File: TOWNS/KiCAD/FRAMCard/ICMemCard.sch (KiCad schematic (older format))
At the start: 15 parts, among them J1 PCMCIA_Connector, Q1 BC846X, Q2 BC846X, U1 FM18W08-SGTR, U2 FM18W08-SGTR

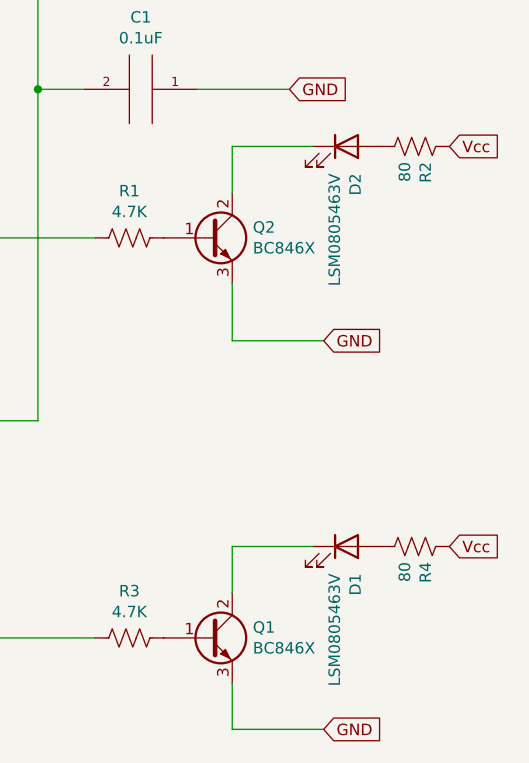
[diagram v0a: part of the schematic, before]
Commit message: Updated resistance.
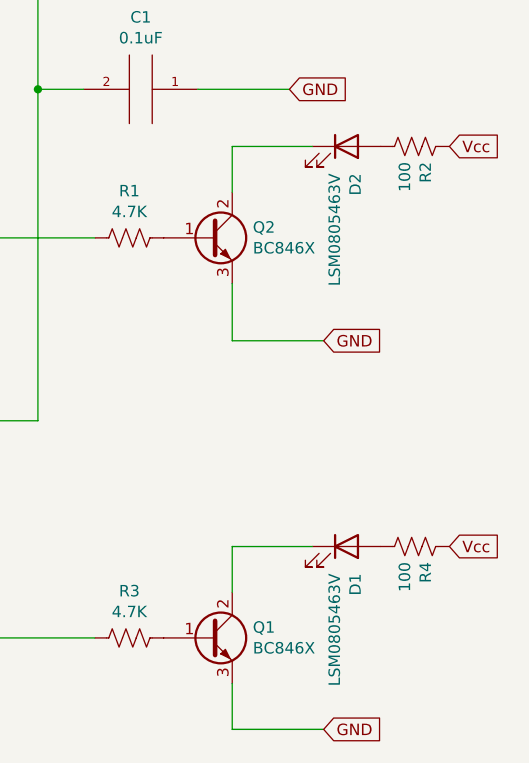
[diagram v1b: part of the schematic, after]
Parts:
- R2, R4: value 80 -> 100
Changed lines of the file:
@@
 P 9800 4300
 F 0 "R4" H 9868 4346 50  0000 L CNN
-F 1 "80" H 9868 4255 50  0000 L CNN
+F 1 "100" H 9868 4255 50  0000 L CNN
 F 2 "PCMCIA:KOA_RK73G2AAT" V 9840 4290 50  0001 C CNN
 F 3 "~" H 9800 4300 50  0001 C CNN
@@
 P 9800 2550
 F 0 "R2" H 9868 2596 50  0000 L CNN
-F 1 "80" H 9868 2505 50  0000 L CNN
+F 1 "100" H 9868 2505 50  0000 L CNN
 F 2 "PCMCIA:KOA_RK73G2AAT" V 9840 2540 50  0001 C CNN
 F 3 "~" H 9800 2550 50  0001 C CNN

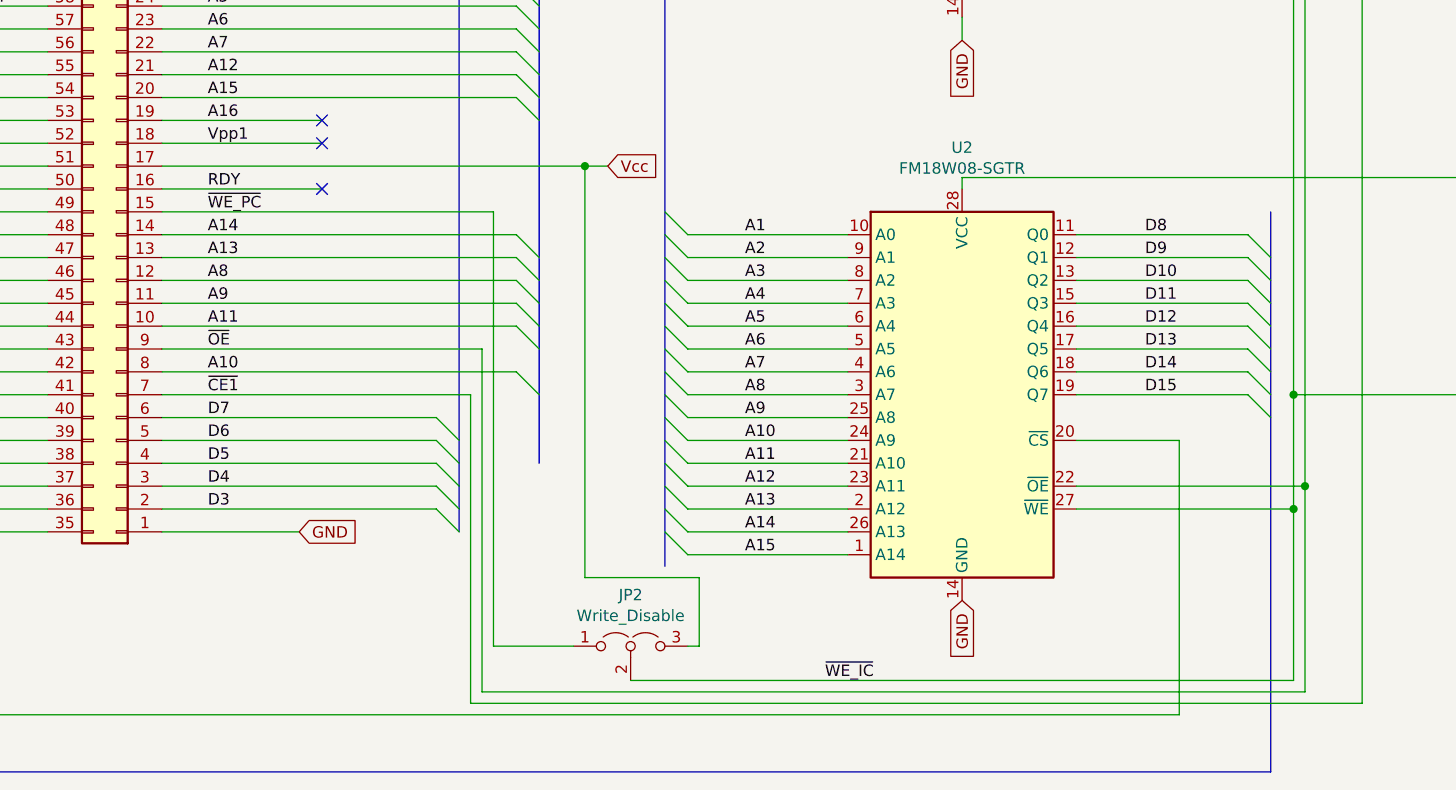
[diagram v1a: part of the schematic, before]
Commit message: Omitted ~WE switch.
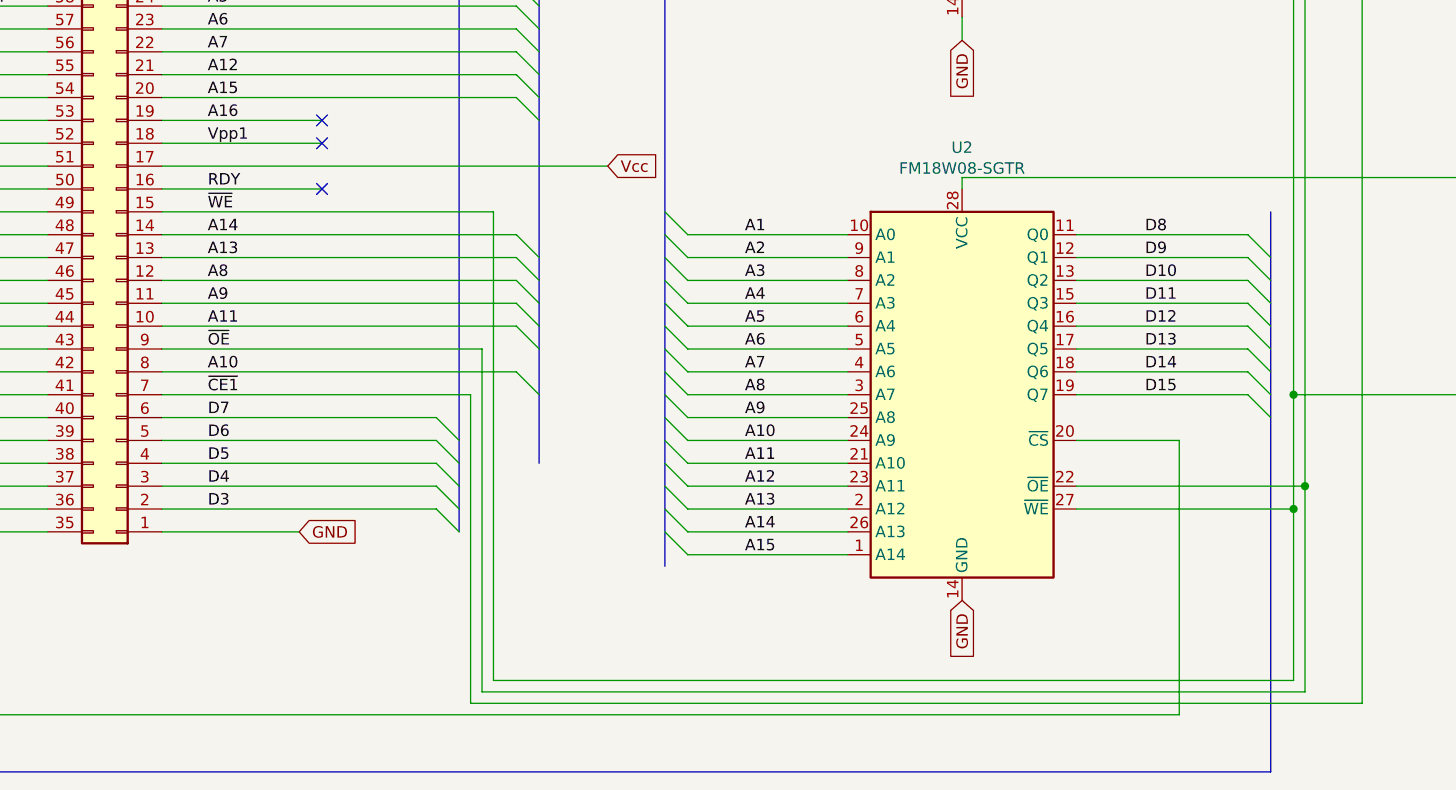
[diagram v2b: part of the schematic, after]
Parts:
- removed JP2: Write_Disable, PCMCIA:MA_Memory_Card_Slide_Switch, symbol Jumper:Jumper_3_Open
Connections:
- net ~WE_PC is gone; now on net ~WE: J1.15 (Pin_15)
- net ~WE_IC renamed ~WE
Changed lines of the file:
@@
 	7400 5950 7400 5200
 Wire Wire Line
-	3900 3900 3900 5800
+	3900 3900 3900 5950
 Wire Wire Line
 	7450 5100 7450 2950
@@
 A14
 Text Label 2650 3900 0    50   ~ 0
-~WE_PC
+~WE
 Text Label 2650 3800 0    50   ~ 0
 RDY
@@
 Wire Wire Line
 	2450 3900 3900 3900
-Wire Wire Line
-	2450 3700 4300 3700
 NoConn ~ 3150 3800
 NoConn ~ 1550 2900
@@
 Wire Wire Line
 	2750 1200 2750 1050
-Text Label 5350 5950 0    50   ~ 0
-~WE_IC
-Wire Wire Line
-	4300 3700 4300 5500
-Connection ~ 4300 3700
-Wire Wire Line
-	4300 3700 4400 3700
-$Comp
-L Jumper:Jumper_3_Open JP2
-U 1 1 62910D29
-P 4500 5800
-F 0 "JP2" H 4500 6024 50  0000 C CNN
-F 1 "Write_Disable" H 4500 5933 50  0000 C CNN
-F 2 "PCMCIA:MA_Memory_Card_Slide_Switch" H 4500 5800 50  0001 C CNN
-F 3 "~" H 4500 5800 50  0001 C CNN
-	1    4500 5800
-	1    0    0    -1
-$EndComp
-Wire Wire Line
-	4800 5800 4750 5800
-Wire Wire Line
-	4250 5800 3900 5800
-Wire Wire Line
-	4500 5950 7400 5950
-Wire Wire Line
-	4800 5800 4800 5500
-Wire Wire Line
-	4800 5500 4300 5500
 $Comp
 L Device:LED D1
@@
 Wire Wire Line
 	8150 1700 8150 2300
+Wire Wire Line
+	2450 3700 4400 3700
+Wire Wire Line
+	3900 5950 7400 5950
 Wire Bus Line
 	3750 950  3750 5300

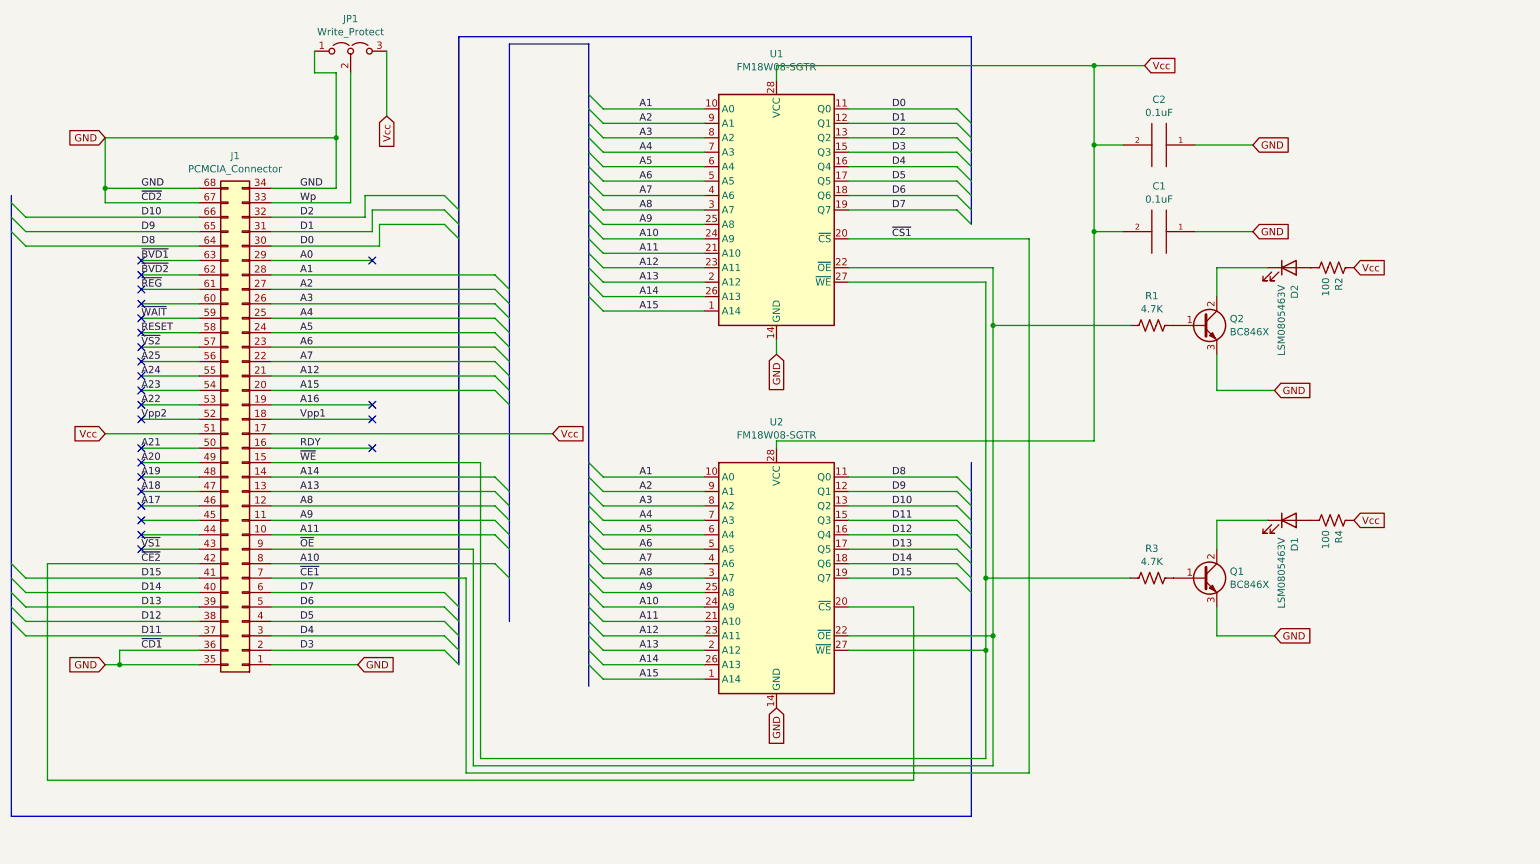
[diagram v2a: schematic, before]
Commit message: Updated FRAM card schematic and PCB.  Added pull-up resistors for ~CE1 and ~CE2 to prevent data corruption on hog-plug and hot-unplug.
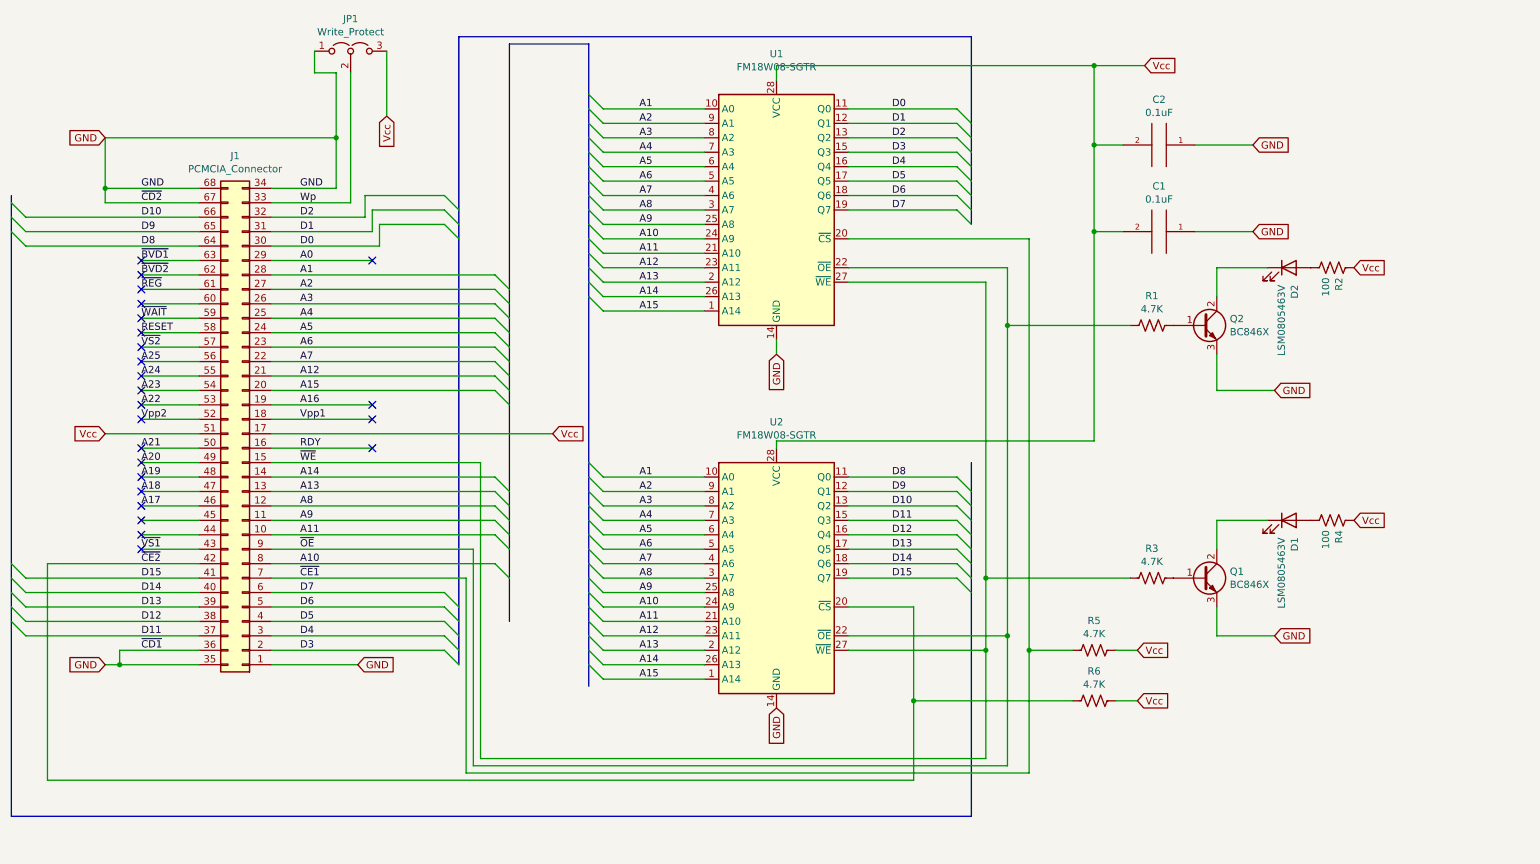
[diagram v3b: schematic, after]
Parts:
- added R5, R6: 4.7K, PCMCIA:KOA_RK73G2AAT, symbol Device:R_US
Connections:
- net Vcc: now also R5.1, R6.1
- net ~CE1: now also R5.2
- net ~CE2: now also R6.2
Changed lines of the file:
@@
 	3900 3900 3900 5950
 Wire Wire Line
-	7450 5100 7450 2950
-Connection ~ 7450 5100
-Wire Wire Line
-	6450 5100 7450 5100
-Wire Wire Line
-	7450 2550 6450 2550
-Wire Wire Line
-	7450 6000 7450 5100
-Wire Wire Line
-	3850 6000 7450 6000
+	7550 5100 7550 2950
+Connection ~ 7550 5100
+Wire Wire Line
+	6450 5100 7550 5100
+Wire Wire Line
+	7550 2550 6450 2550
+Wire Wire Line
+	7550 6000 7550 5100
+Wire Wire Line
+	3850 6000 7550 6000
 Wire Wire Line
 	3850 4500 3850 6000
@@
 	900  4600 1950 4600
 Wire Wire Line
-	6900 4900 6900 6100
-Wire Wire Line
-	7700 2350 7700 6050
+	7700 2350 7700 5200
 Wire Wire Line
 	6450 4900 6900 4900
-Text Label 6750 2350 0    50   ~ 0
-~CS1
 Wire Wire Line
 	2450 4600 4000 4600
@@
 	9000 2550 9000 2750
 Wire Wire Line
-	7450 2950 8400 2950
-Connection ~ 7450 2950
-Wire Wire Line
-	7450 2950 7450 2550
+	7550 2950 8400 2950
+Connection ~ 7550 2950
+Wire Wire Line
+	7550 2950 7550 2550
 Wire Wire Line
 	8400 4700 7400 4700
@@
 Wire Wire Line
 	3900 5950 7400 5950
+$Comp
+L Device:R_US R5
+U 1 1 627E564B
+P 8150 5200
+F 0 "R5" V 7945 5200 50  0000 C CNN
+F 1 "4.7K" V 8036 5200 50  0000 C CNN
+F 2 "PCMCIA:KOA_RK73G2AAT" V 8190 5190 50  0001 C CNN
+F 3 "~" H 8150 5200 50  0001 C CNN
+	1    8150 5200
+	0    1    1    0
+$EndComp
+$Comp
+L Device:R_US R6
+U 1 1 627F2696
+P 8150 5550
+F 0 "R6" V 7945 5550 50  0000 C CNN
+F 1 "4.7K" V 8036 5550 50  0000 C CNN
+F 2 "PCMCIA:KOA_RK73G2AAT" V 8190 5540 50  0001 C CNN
+F 3 "~" H 8150 5550 50  0001 C CNN
+	1    8150 5550
+	0    1    1    0
+$EndComp
+Text GLabel 8450 5200 2    50   Input ~ 0
+Vcc
+Text GLabel 8450 5550 2    50   Input ~ 0
+Vcc
+Wire Wire Line
+	8450 5200 8300 5200
+Wire Wire Line
+	8450 5550 8300 5550
+Wire Wire Line
+	8000 5200 7700 5200
+Connection ~ 7700 5200
+Wire Wire Line
+	7700 5200 7700 6050
+Wire Wire Line
+	8000 5550 6900 5550
+Wire Wire Line
+	6900 4900 6900 5550
+Connection ~ 6900 5550
+Wire Wire Line
+	6900 5550 6900 6100
 Wire Bus Line
 	3750 950  3750 5300

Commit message: Added OR-gate to enforce Write Protection.
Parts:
- added U3: 74AHCT1G32, symbol 74xGxx:74AHCT1G32
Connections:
- net GND: now also U3.3 (GND)
- net Wp: now also U3.1
- net ~WE: now also U3.2; no longer R3.2, U1.27 (~WE), U2.27 (~WE)
- net Vcc renamed VCC
- net VCC: now also U3.5 (VCC)
- new net ~WE~orWP: R3.2, U1.27 (~WE), U2.27 (~WE), U3.4
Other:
- moved on the sheet: D2, Q2, R1, R2, R6
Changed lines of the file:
@@
 	7400 2650 6450 2650
 Wire Wire Line
-	7400 5950 7400 5200
-Wire Wire Line
-	3900 3900 3900 5950
-Wire Wire Line
-	7550 5100 7550 2950
+	7400 5800 7400 5200
+Wire Wire Line
+	3900 3900 3900 5850
+Wire Wire Line
+	7550 5100 7550 3350
 Connection ~ 7550 5100
 Wire Wire Line
@@
 	2450 4800 3650 4800
 Entry Wire Line
-	3650 2250 3750 2350
-Entry Wire Line
-	3650 2150 3750 2250
-Entry Wire Line
-	3650 2050 3750 2150
-Wire Wire Line
-	2450 2400 3200 2400
-Wire Wire Line
-	3200 2250 3650 2250
-Wire Wire Line
-	3200 2400 3200 2250
-Wire Wire Line
-	2450 2300 3150 2300
-Wire Wire Line
-	3150 2150 3650 2150
-Wire Wire Line
-	3150 2300 3150 2150
-Wire Wire Line
-	2450 2200 3100 2200
-Wire Wire Line
-	3100 2050 3650 2050
-Wire Wire Line
-	3100 2200 3100 2050
+	3650 2400 3750 2500
+Entry Wire Line
+	3650 2300 3750 2400
+Entry Wire Line
+	3650 2200 3750 2300
 Wire Wire Line
 	2900 2000 2450 2000
@@
 Text GLabel 1300 3700 0    50   Input ~ 0
 Vcc
-Text GLabel 4400 3700 2    50   Input ~ 0
+Text GLabel 3450 3700 2    50   Input ~ 0
 Vcc
 $Comp
@@
 Entry Wire Line
 	4000 3400 4100 3500
-Text GLabel 5950 5600 3    50   Input ~ 0
+Text GLabel 5900 5650 0    50   Input ~ 0
 GND
 Text GLabel 5950 3150 3    50   Input ~ 0
@@
 Wire Wire Line
 	2450 4700 3800 4700
-Wire Wire Line
-	2450 5300 3050 5300
 Wire Wire Line
 	2450 4500 3850 4500
@@
 NoConn ~ 1550 4500
 Wire Wire Line
-	3000 2100 3000 1200
-Wire Wire Line
 	2450 2100 3000 2100
 Wire Wire Line
@@
 L Device:Q_NPN_BCE Q2
 U 1 1 625E875F
-P 8900 2950
-F 0 "Q2" H 9090 2996 50  0000 L CNN
-F 1 "BC846X" H 9090 2905 50  0000 L CNN
-F 2 "PCMCIA:BC846X_AU_Q_NPN_BCE" H 9100 3050 50  0001 C CNN
-F 3 "~" H 8900 2950 50  0001 C CNN
-	1    8900 2950
+P 8900 3350
+F 0 "Q2" H 9090 3396 50  0000 L CNN
+F 1 "BC846X" H 9090 3305 50  0000 L CNN
+F 2 "PCMCIA:BC846X_AU_Q_NPN_BCE" H 9100 3450 50  0001 C CNN
+F 3 "~" H 8900 3350 50  0001 C CNN
+	1    8900 3350
 	1    0    0    -1
 $EndComp
@@
 L Device:R_US R1
 U 1 1 626373D3
-P 8550 2950
-F 0 "R1" V 8345 2950 50  0000 C CNN
-F 1 "4.7K" V 8436 2950 50  0000 C CNN
-F 2 "PCMCIA:KOA_RK73G2AAT" V 8590 2940 50  0001 C CNN
-F 3 "~" H 8550 2950 50  0001 C CNN
-	1    8550 2950
+P 8550 3350
+F 0 "R1" V 8345 3350 50  0000 C CNN
+F 1 "4.7K" V 8436 3350 50  0000 C CNN
+F 2 "PCMCIA:KOA_RK73G2AAT" V 8590 3340 50  0001 C CNN
+F 3 "~" H 8550 3350 50  0001 C CNN
+	1    8550 3350
 	0    1    1    0
 $EndComp
@@
 L Device:R_US R2
 U 1 1 62637FF1
-P 9800 2550
-F 0 "R2" H 9868 2596 50  0000 L CNN
-F 1 "100" H 9868 2505 50  0000 L CNN
-F 2 "PCMCIA:KOA_RK73G2AAT" V 9840 2540 50  0001 C CNN
-F 3 "~" H 9800 2550 50  0001 C CNN
-	1    9800 2550
+P 9800 2950
+F 0 "R2" H 9868 2996 50  0000 L CNN
+F 1 "100" H 9868 2905 50  0000 L CNN
+F 2 "PCMCIA:KOA_RK73G2AAT" V 9840 2940 50  0001 C CNN
+F 3 "~" H 9800 2950 50  0001 C CNN
+	1    9800 2950
 	0    1    1    0
 $EndComp
 Wire Wire Line
-	9000 3400 9400 3400
-Text GLabel 9400 3400 2    50   Input ~ 0
+	9000 3800 9400 3800
+Text GLabel 9400 3800 2    50   Input ~ 0
 GND
 Wire Wire Line
@@
 GND
 Wire Wire Line
-	9000 3400 9000 3150
+	9000 3800 9000 3550
 Wire Wire Line
 	9000 5100 9000 4900
-Text GLabel 9950 2550 2    50   Input ~ 0
+Text GLabel 9950 2950 2    50   Input ~ 0
 Vcc
 Wire Wire Line
@@
 	9000 4300 9000 4500
 Wire Wire Line
-	9000 2550 9000 2750
-Wire Wire Line
-	7550 2950 8400 2950
-Connection ~ 7550 2950
-Wire Wire Line
-	7550 2950 7550 2550
+	9000 2950 9000 3150
+Wire Wire Line
+	7550 3350 8400 3350
 Wire Wire Line
 	8400 4700 7400 4700
@@
 	7400 4700 7400 2650
 Wire Wire Line
-	9000 2550 9350 2550
+	9000 2950 9350 2950
 $Comp
 L Device:LED D2
 U 1 1 625C2726
-P 9500 2550
-F 0 "D2" V 9539 2432 50  0000 R CNN
-F 1 "LSM0805463V" V 9448 2432 50  0000 R CNN
-F 2 "PCMCIA:LSM0805463V" H 9500 2550 50  0001 C CNN
-F 3 "~" H 9500 2550 50  0001 C CNN
-	1    9500 2550
+P 9500 2950
+F 0 "D2" V 9539 2832 50  0000 R CNN
+F 1 "LSM0805463V" V 9448 2832 50  0000 R CNN
+F 2 "PCMCIA:LSM0805463V" H 9500 2950 50  0001 C CNN
+F 3 "~" H 9500 2950 50  0001 C CNN
+	1    9500 2950
 	1    0    0    -1
 $EndComp
@@
 	8150 1700 8150 2300
 Wire Wire Line
-	2450 3700 4400 3700
-Wire Wire Line
-	3900 5950 7400 5950
+	2450 3700 3450 3700
 $Comp
 L Device:R_US R5
@@
 L Device:R_US R6
 U 1 1 627F2696
-P 8150 5550
-F 0 "R6" V 7945 5550 50  0000 C CNN
-F 1 "4.7K" V 8036 5550 50  0000 C CNN
-F 2 "PCMCIA:KOA_RK73G2AAT" V 8190 5540 50  0001 C CNN
-F 3 "~" H 8150 5550 50  0001 C CNN
-	1    8150 5550
+P 8150 6100
+F 0 "R6" V 7945 6100 50  0000 C CNN
+F 1 "4.7K" V 8036 6100 50  0000 C CNN
+F 2 "PCMCIA:KOA_RK73G2AAT" V 8190 6090 50  0001 C CNN
+F 3 "~" H 8150 6100 50  0001 C CNN
+	1    8150 6100
 	0    1    1    0
 $EndComp
 Text GLabel 8450 5200 2    50   Input ~ 0
 Vcc
-Text GLabel 8450 5550 2    50   Input ~ 0
+Text GLabel 8450 6100 2    50   Input ~ 0
 Vcc
 Wire Wire Line
 	8450 5200 8300 5200
 Wire Wire Line
-	8450 5550 8300 5550
+	8450 6100 8300 6100
 Wire Wire Line
 	8000 5200 7700 5200
@@
 	7700 5200 7700 6050
 Wire Wire Line
-	8000 5550 6900 5550
-Wire Wire Line
-	6900 4900 6900 5550
-Connection ~ 6900 5550
-Wire Wire Line
-	6900 5550 6900 6100
+	8000 6100 6900 6100
+$Comp
+L 74xGxx:74AHCT1G32 U3
+U 1 1 62849B15
+P 4750 5800
+F 0 "U3" H 4725 6067 50  0000 C CNN
+F 1 "74AHCT1G32" H 4725 5976 50  0000 C CNN
+F 2 "" H 4750 5800 50  0001 C CNN
+F 3 "http://www.ti.com/lit/sg/scyt129e/scyt129e.pdf" H 4750 5800 50  0001 C CNN
+	1    4750 5800
+	1    0    0    -1
+$EndComp
+Wire Wire Line
+	3000 2100 4250 2100
+Wire Wire Line
+	4250 5750 4450 5750
+Connection ~ 3000 2100
+Wire Wire Line
+	3000 2100 3000 1200
+Wire Wire Line
+	3900 5850 4450 5850
+Wire Wire Line
+	5000 5800 7400 5800
+Text Label 5150 5800 0    50   ~ 0
+~WE~orWP
+Wire Wire Line
+	4250 2100 4250 5750
+Wire Wire Line
+	2450 2400 3650 2400
+Wire Wire Line
+	2450 2300 3650 2300
+Wire Wire Line
+	2450 2200 3650 2200
+Wire Wire Line
+	2450 5300 3050 5300
+Text GLabel 4850 5950 2    50   Input ~ 0
+GND
+Text GLabel 5000 5600 2    50   Input ~ 0
+Vcc
+Wire Wire Line
+	5000 5600 4750 5600
+Wire Wire Line
+	4750 5600 4750 5700
+Wire Wire Line
+	4850 5950 4750 5950
+Wire Wire Line
+	4750 5950 4750 5900
+Wire Wire Line
+	5900 5650 5950 5650
+Wire Wire Line
+	5950 5650 5950 5600
+Connection ~ 6900 6100
+Wire Wire Line
+	6900 4900 6900 6100
+Connection ~ 7550 3350
+Wire Wire Line
+	7550 2550 7550 3350
 Wire Bus Line
 	3750 950  3750 5300
